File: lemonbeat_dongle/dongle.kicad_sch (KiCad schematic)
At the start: 0 parts

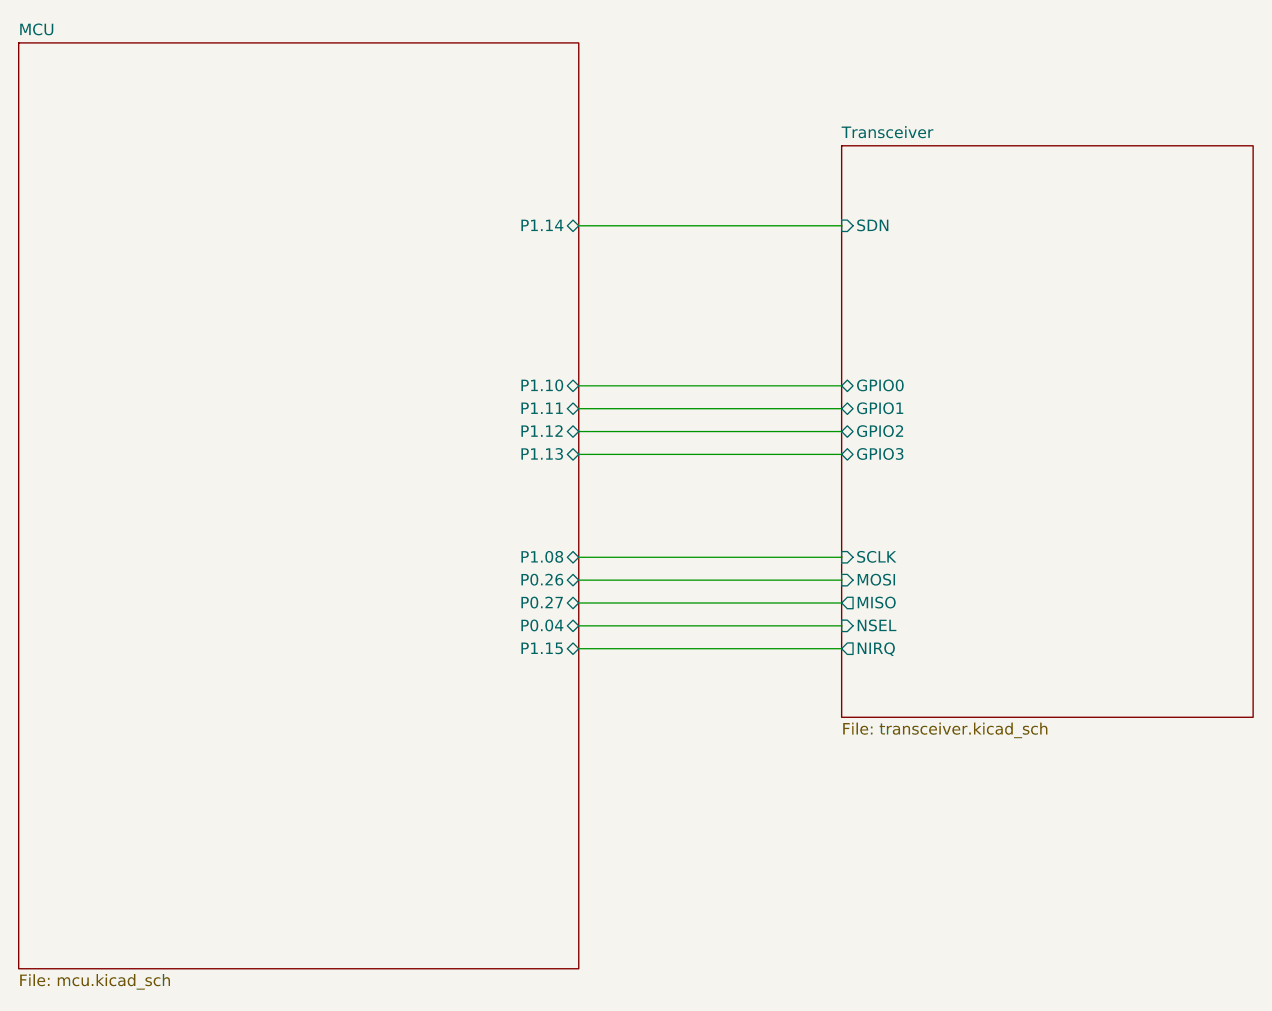
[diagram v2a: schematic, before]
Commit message: dongle: use pins on outer rows of nRF52840
Replace pins on inner row with pins on outer row to facilitate
routing.

All pins for communication with Si4467 are non low-drive pins.
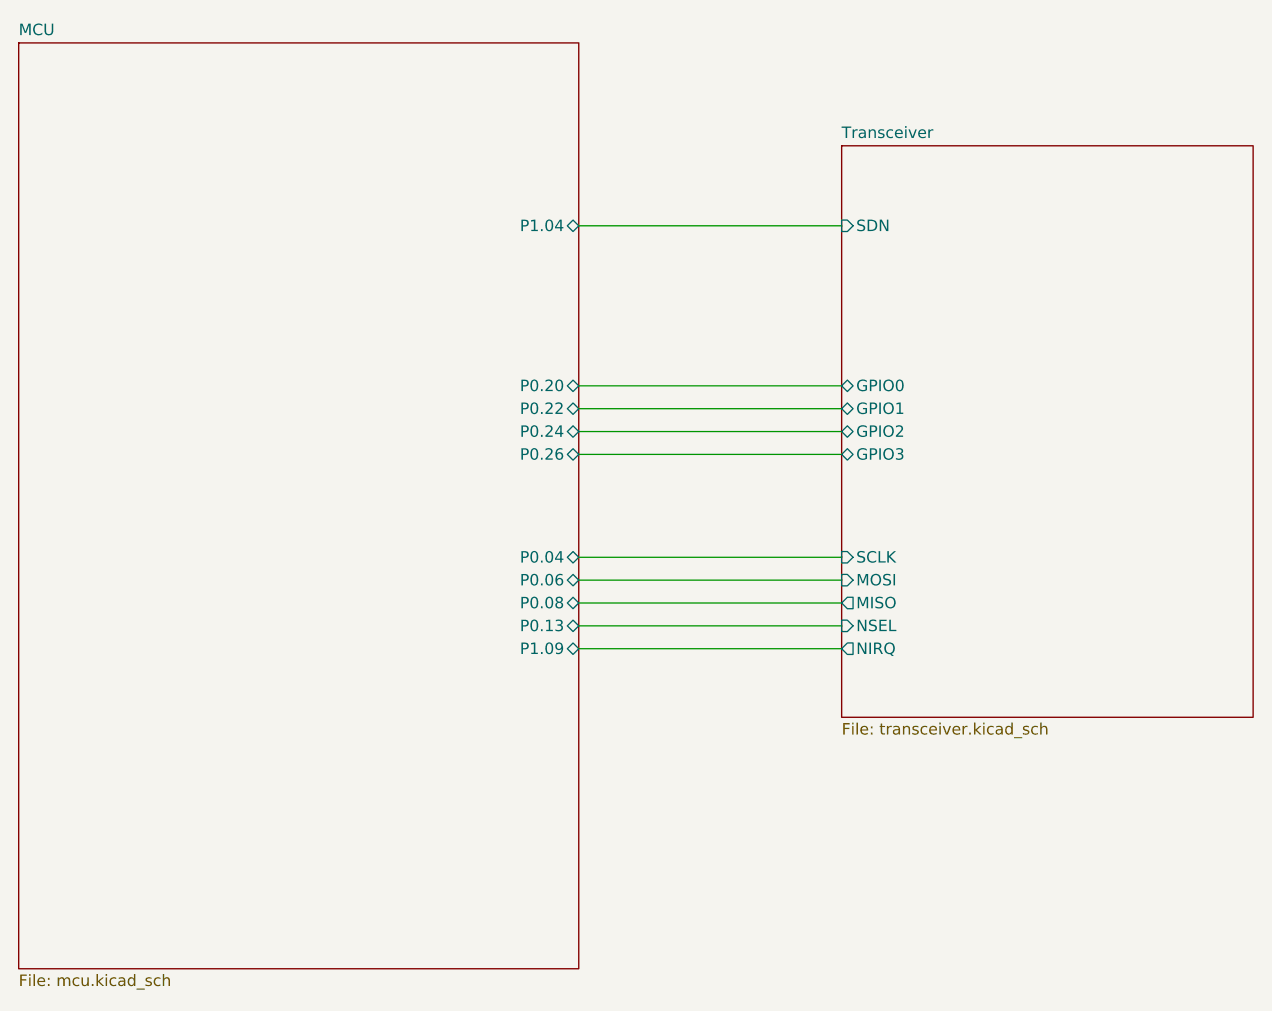
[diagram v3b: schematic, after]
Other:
- sheet MCU ports: added P0.06, P0.08, P0.13, P0.20, P0.22, P0.24, P1.04, P1.09; removed P0.27, P1.08, P1.10, P1.11, P1.12, P1.13, P1.14, P1.15
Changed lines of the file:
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@@
     (rev "0.1.0")
+  )
+  (wire (pts (xy 116.84 97.79) (xy 146.05 97.79))
+    (stroke (width 0) (type default) (color 0 0 0 0))
+  )
+  (wire (pts (xy 116.84 116.84) (xy 146.05 116.84))
+    (stroke (width 0) (type default) (color 0 0 0 0))
+  )
+  (wire (pts (xy 116.84 95.25) (xy 146.05 95.25))
+    (stroke (width 0) (type default) (color 0 0 0 0))
+  )
+  (wire (pts (xy 116.84 72.39) (xy 146.05 72.39))
+    (stroke (width 0) (type default) (color 0 0 0 0))
+  )
+  (wire (pts (xy 116.84 114.3) (xy 146.05 114.3))
+    (stroke (width 0) (type default) (color 0 0 0 0))
+  )
+  (wire (pts (xy 116.84 92.71) (xy 146.05 92.71))
+    (stroke (width 0) (type default) (color 0 0 0 0))
   )
   (wire (pts (xy 116.84 90.17) (xy 146.05 90.17))
     (stroke (width 0) (type default) (color 0 0 0 0))
   )
-  (wire (pts (xy 116.84 119.38) (xy 146.05 119.38))
+  (wire (pts (xy 116.84 109.22) (xy 146.05 109.22))
     (stroke (width 0) (type default) (color 0 0 0 0))
   )
@@
     (stroke (width 0) (type default) (color 0 0 0 0))
   )
-  (wire (pts (xy 116.84 109.22) (xy 146.05 109.22))
-    (stroke (width 0) (type default) (color 0 0 0 0))
-  )
-  (wire (pts (xy 116.84 92.71) (xy 146.05 92.71))
-    (stroke (width 0) (type default) (color 0 0 0 0))
-  )
-  (wire (pts (xy 116.84 114.3) (xy 146.05 114.3))
-    (stroke (width 0) (type default) (color 0 0 0 0))
-  )
-  (wire (pts (xy 116.84 72.39) (xy 146.05 72.39))
-    (stroke (width 0) (type default) (color 0 0 0 0))
-  )
-  (wire (pts (xy 116.84 97.79) (xy 146.05 97.79))
-    (stroke (width 0) (type default) (color 0 0 0 0))
-  )
-  (wire (pts (xy 116.84 95.25) (xy 146.05 95.25))
-    (stroke (width 0) (type default) (color 0 0 0 0))
-  )
-  (wire (pts (xy 116.84 116.84) (xy 146.05 116.84))
+  (wire (pts (xy 116.84 119.38) (xy 146.05 119.38))
     (stroke (width 0) (type default) (color 0 0 0 0))
   )
@@
       (effects (font (size 1.27 1.27)) (justify left top))
     )
-    (pin "P1.12" bidirectional (at 116.84 95.25 0)
+    (pin "P0.26" bidirectional (at 116.84 97.79 0)
       (effects (font (size 1.27 1.27)) (justify right))
     )
-    (pin "P1.15" bidirectional (at 116.84 119.38 0)
+    (pin "P0.04" bidirectional (at 116.84 109.22 0)
       (effects (font (size 1.27 1.27)) (justify right))
     )
-    (pin "P1.13" bidirectional (at 116.84 97.79 0)
+    (pin "P1.04" bidirectional (at 116.84 72.39 0)
       (effects (font (size 1.27 1.27)) (justify right))
     )
-    (pin "P1.11" bidirectional (at 116.84 92.71 0)
+    (pin "P0.22" bidirectional (at 116.84 92.71 0)
       (effects (font (size 1.27 1.27)) (justify right))
     )
-    (pin "P1.10" bidirectional (at 116.84 90.17 0)
+    (pin "P0.20" bidirectional (at 116.84 90.17 0)
       (effects (font (size 1.27 1.27)) (justify right))
     )
-    (pin "P1.14" bidirectional (at 116.84 72.39 0)
+    (pin "P1.09" bidirectional (at 116.84 119.38 0)
       (effects (font (size 1.27 1.27)) (justify right))
     )
-    (pin "P1.08" bidirectional (at 116.84 109.22 0)
+    (pin "P0.13" bidirectional (at 116.84 116.84 0)
       (effects (font (size 1.27 1.27)) (justify right))
     )
-    (pin "P0.26" bidirectional (at 116.84 111.76 0)
+    (pin "P0.24" bidirectional (at 116.84 95.25 0)
       (effects (font (size 1.27 1.27)) (justify right))
     )
-    (pin "P0.27" bidirectional (at 116.84 114.3 0)
+    (pin "P0.06" bidirectional (at 116.84 111.76 0)
       (effects (font (size 1.27 1.27)) (justify right))
     )
-    (pin "P0.04" bidirectional (at 116.84 116.84 0)
+    (pin "P0.08" bidirectional (at 116.84 114.3 0)
       (effects (font (size 1.27 1.27)) (justify right))
     )

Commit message: dongle: add some test points
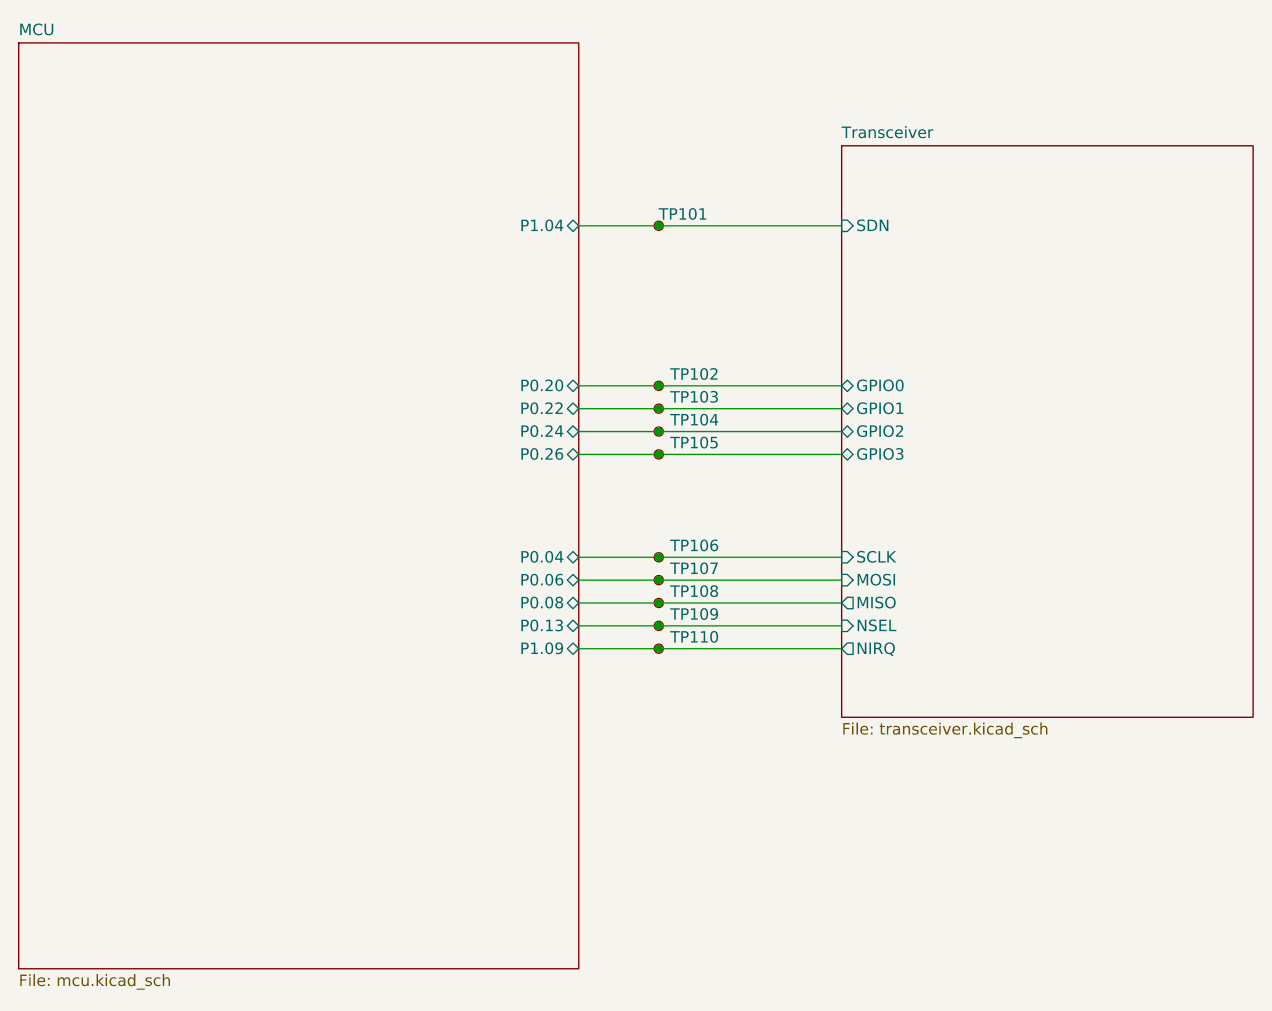
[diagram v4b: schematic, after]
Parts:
- added TP101, TP102, TP103, TP104, TP105, TP106, TP107, TP108, TP109, TP110: TestPoint_Small, TestPoint:TestPoint_Pad_D1.0mm, symbol Connector:TestPoint_Small
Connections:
- net MCU/P0.04: now also TP106.1
- net MCU/P0.06: now also TP107.1
- net MCU/P0.08: now also TP108.1
- net MCU/P0.13: now also TP109.1
- net MCU/P0.20: now also TP102.1
- net MCU/P0.22: now also TP103.1
- net MCU/P0.24: now also TP104.1
- net MCU/P0.26: now also TP105.1
- net MCU/P1.04: now also TP101.1
- net MCU/P1.09: now also TP110.1

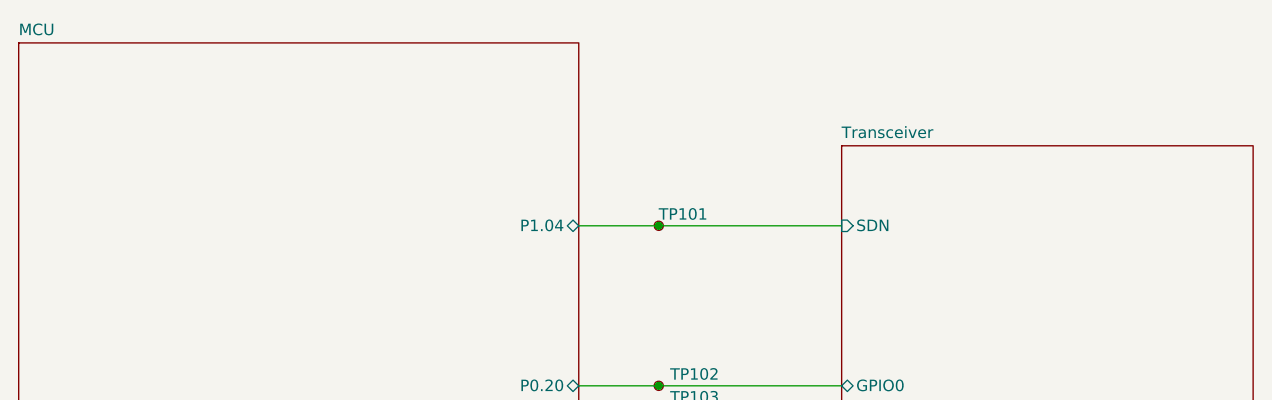
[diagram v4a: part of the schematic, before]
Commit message: dongle: schematic: notes & cosmetic changes
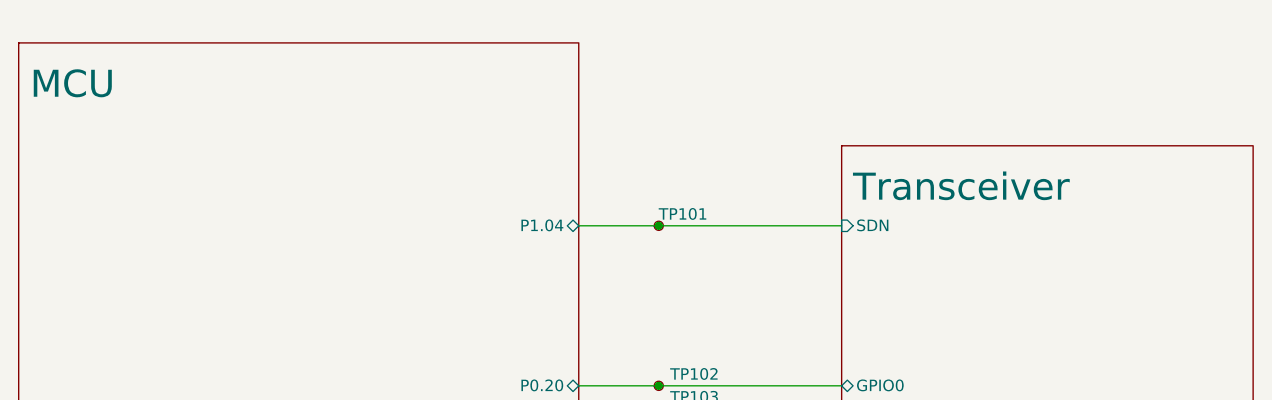
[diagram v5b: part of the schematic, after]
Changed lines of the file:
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@@
     (pin "1")
   )
-  (sheet (at 54.61 52.07) (size 62.23 102.87) (fields_autoplaced)
+  (sheet (at 54.61 52.07) (size 62.23 102.87)
     (stroke (width 0.1524) (type solid) (color 0 0 0 0))
     (fill (color 0 0 0 0.0000))
-    (property "Sheet name" "MCU" (id 0) (at 54.61 51.3584 0)
-      (effects (font (size 1.27 1.27)) (justify left bottom))
+    (property "Sheet name" "MCU" (id 0) (at 55.88 58.42 0)
+      (effects (font (size 3 3)) (justify left bottom))
     )
     (property "Sheet file" "mcu.kicad_sch" (id 1) (at 54.61 155.5246 0)
@@
     )
   )
-  (sheet (at 146.05 63.5) (size 45.72 63.5) (fields_autoplaced)
+  (sheet (at 146.05 63.5) (size 45.72 63.5)
     (stroke (width 0.1524) (type solid) (color 0 0 0 0))
     (fill (color 0 0 0 0.0000))
-    (property "Sheet name" "Transceiver" (id 0) (at 146.05 62.7884 0)
-      (effects (font (size 1.27 1.27)) (justify left bottom))
+    (property "Sheet name" "Transceiver" (id 0) (at 147.32 69.85 0)
+      (effects (font (size 3 3)) (justify left bottom))
     )
     (property "Sheet file" "transceiver.kicad_sch" (id 1) (at 146.05 127.5846 0)
@@
       (reference "#FLG0105") (unit 1) (value "PWR_FLAG") (footprint "")
     )
-    (path "/49f47eff-be71-45a3-baa2-ec3b29bb6923/cfdc75eb-93c6-4da5-9108-6acf0b01f5f0"
-      (reference "#FLG0106") (unit 1) (value "PWR_FLAG") (footprint "")
-    )
     (path "/7368be1f-88e3-4616-a1f9-4c1e3857cf01/90ea6193-1bce-4f59-8a1f-22eb3a025089"
